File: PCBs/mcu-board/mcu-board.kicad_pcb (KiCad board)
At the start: 2 copper layers, 6 parts, among them J1 ENCODER-PANEL-1, J2 ENCODER-PANEL-2, J3 5V, J4 3.3V, J5 MDAC-INPUT-SELECTOR, U1 m0-express

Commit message: Updating mcu-board PCB
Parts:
- removed J3: 5V, Connector_Molex:Molex_KK-254_AE-6410-02A_1x02_P2.54mm_Vertical
- removed J4: 3.3V, Connector_Molex:Molex_KK-254_AE-6410-02A_1x02_P2.54mm_Vertical
- added 3.3V1: 3.3V, Connector_Molex:Molex_KK-254_AE-6410-02A_1x02_P2.54mm_Vertical, F.Cu at (153.7, 67.9)
- added 5V1: 5V, Connector_Molex:Molex_KK-254_AE-6410-02A_1x02_P2.54mm_Vertical, F.Cu at (187.3, 60.3)
- added C1: C, Capacitor_SMD:C_1206_3216Metric_Pad1.42x1.75mm_HandSolder, B.Cu at (189.2, 87.6)
- added C2: C, Capacitor_SMD:C_1206_3216Metric_Pad1.42x1.75mm_HandSolder, F.Cu at (181.6, 76.8)
- added H1: MountingHole_Pad, MountingHole:MountingHole_3.2mm_M3_Pad, F.Cu at (194.5, 100.0)
- added H2: MountingHole_Pad, MountingHole:MountingHole_3.2mm_M3_Pad, F.Cu at (153.0, 100.0)
- added H3: MountingHole_Pad, MountingHole:MountingHole_3.2mm_M3_Pad, F.Cu at (194.5, 60.0)
- added H4: MountingHole_Pad, MountingHole:MountingHole_3.2mm_M3_Pad, F.Cu at (153.0, 60.0)
- added IR1: Conn_01x03, Connector_Molex:Molex_KK-254_AE-6410-03A_1x03_P2.54mm_Vertical, F.Cu at (181.0, 67.9)
- added LED_3V1: LED, LED_SMD:LED_1206_3216Metric_Pad1.42x1.75mm_HandSolder, F.Cu at (161.9, 59.1)
- added LED_5V1: LED, LED_SMD:LED_1206_3216Metric_Pad1.42x1.75mm_HandSolder, F.Cu at (172.7, 59.1)
- added RLED1: R, Resistor_SMD:R_1206_3216Metric_Pad1.42x1.75mm_HandSolder, F.Cu at (161.9, 62.9)
- added RLED2: R, Resistor_SMD:R_1206_3216Metric_Pad1.42x1.75mm_HandSolder, F.Cu at (172.7, 62.9)
- added U2: SN74AHCT125DR, Package_SO:SOIC-14_3.9x8.7mm_P1.27mm, F.Cu at (184.2, 87.6)
- added U3: SN74AHCT125DR, Package_SO:SOIC-14_3.9x8.7mm_P1.27mm, B.Cu at (184.2, 76.8)
- added VBAT1: V-BAT, Connector_Molex:Molex_KK-254_AE-6410-02A_1x02_P2.54mm_Vertical, F.Cu at (181.0, 60.3)
- moved J1 75.8 mm to (194.3, 82.5), turned to 270 degrees
- moved J2 64.2 mm to (194.3, 67.3), turned to 270 degrees
- moved J5 35.3 mm to (153.7, 80.6), turned to 270 degrees
- moved U1 0.23 mm to (167.6, 85.7)
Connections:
- J1 pad 1: Net-(J1-Pad1) -> GND
- J1 pad 2: Net-(J1-Pad2) -> +5V
- J1 pad 3: Net-(J1-Pad3) -> encoder_1_neopixel_5v
- J1 pad 4: Net-(J1-Pad4) -> encoder_1_A_5v
- J1 pad 5: Net-(J1-Pad5) -> encoder_1_B_5v
- J2 pad 1: Net-(J2-Pad1) -> GND
- J2 pad 2: Net-(J2-Pad2) -> +5V
- J2 pad 3: Net-(J2-Pad3) -> encoder_2_neopixel_5v
- J2 pad 4: Net-(J2-Pad4) -> encoder_2_A_5v
- J2 pad 5: Net-(J2-Pad5) -> encoder_2_B_5v
- J5 pad 1: Net-(J5-Pad1) -> GND
- J5 pad 2: Net-(J5-Pad2) -> +3V3
- J5 pad 3: Net-(J5-Pad3) -> CS_input_selector
- J5 pad 4: Net-(J5-Pad4) -> SCK
- J5 pad 5: Net-(J5-Pad5) -> CS_mdac_attenuator
- J5 pad 6: Net-(J5-Pad6) -> MOSI
- U1 pad 10: Net-(U1-Pad10) -> CS_mdac_attenuator
- U1 pad 11: Net-(U1-Pad11) -> SCK
- U1 pad 12: Net-(U1-Pad12) -> MOSI
- U1 pad 19: Net-(U1-Pad19) -> encoder_1_B_3v
- U1 pad 2: Net-(U1-Pad2) -> +3V3
- U1 pad 20: Net-(U1-Pad20) -> encoder_1_A_3v
- U1 pad 21: Net-(U1-Pad21) -> encoder_1_neopixel_3v
- U1 pad 22: Net-(U1-Pad22) -> encoder_2_B_3v
- U1 pad 23: Net-(U1-Pad23) -> encoder_2_A_3v
- U1 pad 24: Net-(U1-Pad24) -> encoder_2_neopixel_3v
- U1 pad 25: Net-(U1-Pad25) -> IR_SENSOR
- U1 pad 26: Net-(U1-Pad26) -> +5V
- U1 pad 27: Net-(U1-Pad27) -> GND
- U1 pad 28: Net-(U1-Pad28) -> BAT
- U1 pad 9: Net-(U1-Pad9) -> CS_input_selector
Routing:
- net +3V3: track 0.00 -> 117.7 mm, vias 0 -> 1
- net +5V: track 0.00 -> 72.9 mm, vias 0 -> 1
- net encoder_1_neopixel_5v: track 0.00 -> 18.1 mm
- net encoder_2_neopixel_5v: track 0.00 -> 16.5 mm
- net encoder_2_A_5v: track 0.00 -> 16.2 mm
- net encoder_1_A_5v: track 0.00 -> 15.2 mm
- net IR_SENSOR: track 0.00 -> 15.1 mm
- net encoder_1_neopixel_3v: track 0.00 -> 14.6 mm
- net encoder_2_B_3v: track 0.00 -> 13.4 mm
- net BAT: track 0.00 -> 12.2 mm
- net encoder_2_B_5v: track 0.00 -> 11.4 mm
- net encoder_1_B_3v: track 0.00 -> 11.3 mm
- net encoder_1_B_5v: track 0.00 -> 10.5 mm
- net encoder_2_neopixel_3v: track 0.00 -> 10.3 mm
- net SCK: track 0.00 -> 9.57 mm
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- added copper zone on B.Cu, net GND
- added copper zone on F.Cu, net GND
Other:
- board outline added: 50.5 x 49 mm
- net class Default: clearance 0.2 -> 0.1524; trace_width 0.25 -> 0.4
- net class power added: clearance 0.1524, trace_width 0.7, via_dia 0.8, via_drill 0.4
- rule trace_clearance: 0.2 -> 0.1524

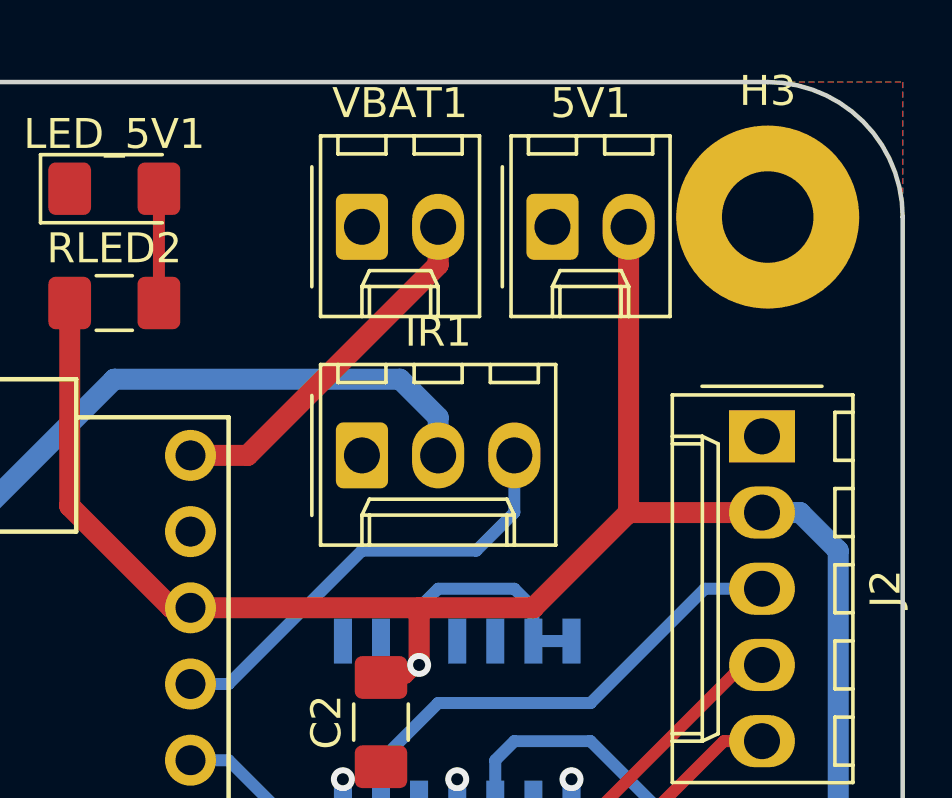
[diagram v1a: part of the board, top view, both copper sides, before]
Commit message: renaming some nets
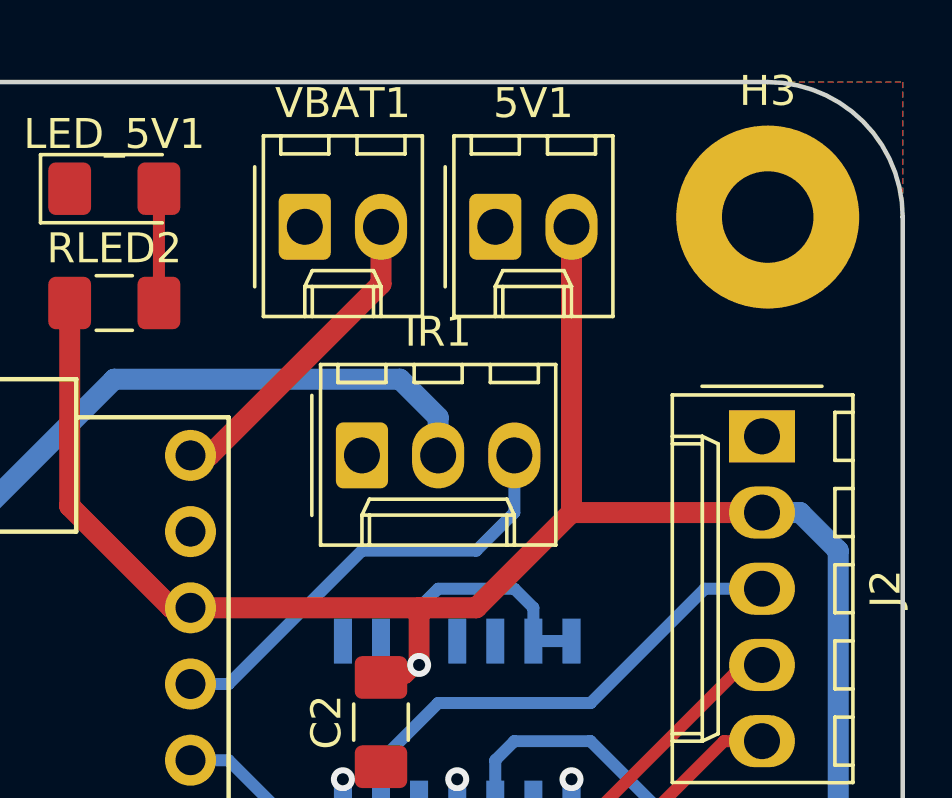
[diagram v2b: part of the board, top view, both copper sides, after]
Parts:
- moved 5V1 1.91 mm to (185.4, 60.3)
- moved VBAT1 1.91 mm to (179.1, 60.3)
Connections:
- net encoder_1_A_3v renamed panel_1_encoder_A_3v
- net encoder_1_A_5v renamed panel_1_encoder_A_5v
- net encoder_1_B_3v renamed panel_1_encoder_B_3v
- net encoder_1_B_5v renamed panel_1_encoder_B_5v
- net encoder_1_neopixel_3v renamed panel_1_neopixel_3v
- net encoder_1_neopixel_5v renamed panel_1_neopixel_5v
- net encoder_2_A_3v renamed panel_2_encoder_A_3v
- net encoder_2_A_5v renamed panel_2_encoder_A_5v
- net encoder_2_B_3v renamed panel_2_encoder_B_3v
- net encoder_2_B_5v renamed panel_2_encoder_B_5v
- net encoder_2_neopixel_3v renamed panel_2_neopixel_3v
- net encoder_2_neopixel_5v renamed panel_2_neopixel_5v
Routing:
- net BAT: track 12.2 -> 10.6 mm

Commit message: starting to fix silkscreen
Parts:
- removed J1: ENCODER-PANEL-1, Connector_Molex:Molex_KK-254_AE-6410-05A_1x05_P2.54mm_Vertical
- removed J2: ENCODER-PANEL-2, Connector_Molex:Molex_KK-254_AE-6410-05A_1x05_P2.54mm_Vertical
- added ENCODER-PANEL-1: ENCODER-PANEL-1, Connector_Molex:Molex_KK-254_AE-6410-05A_1x05_P2.54mm_Vertical, F.Cu at (194.3, 82.5)
- added ENCODER-PANEL-2: ENCODER-PANEL-2, Connector_Molex:Molex_KK-254_AE-6410-05A_1x05_P2.54mm_Vertical, F.Cu at (194.3, 67.3)
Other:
- rule trace_min: 0.2 -> 0.1524
- rule via_min_drill: 0.3 -> 0.3302
- rule via_min_size: 0.4 -> 0.6858
- board text added: "Adafruit ItsyBitsy M0 Express"
- board text added: "attenuator/selector"
- board text added: "futuresharks@gmail.com"
- board text added: "mcu-board v1.0"

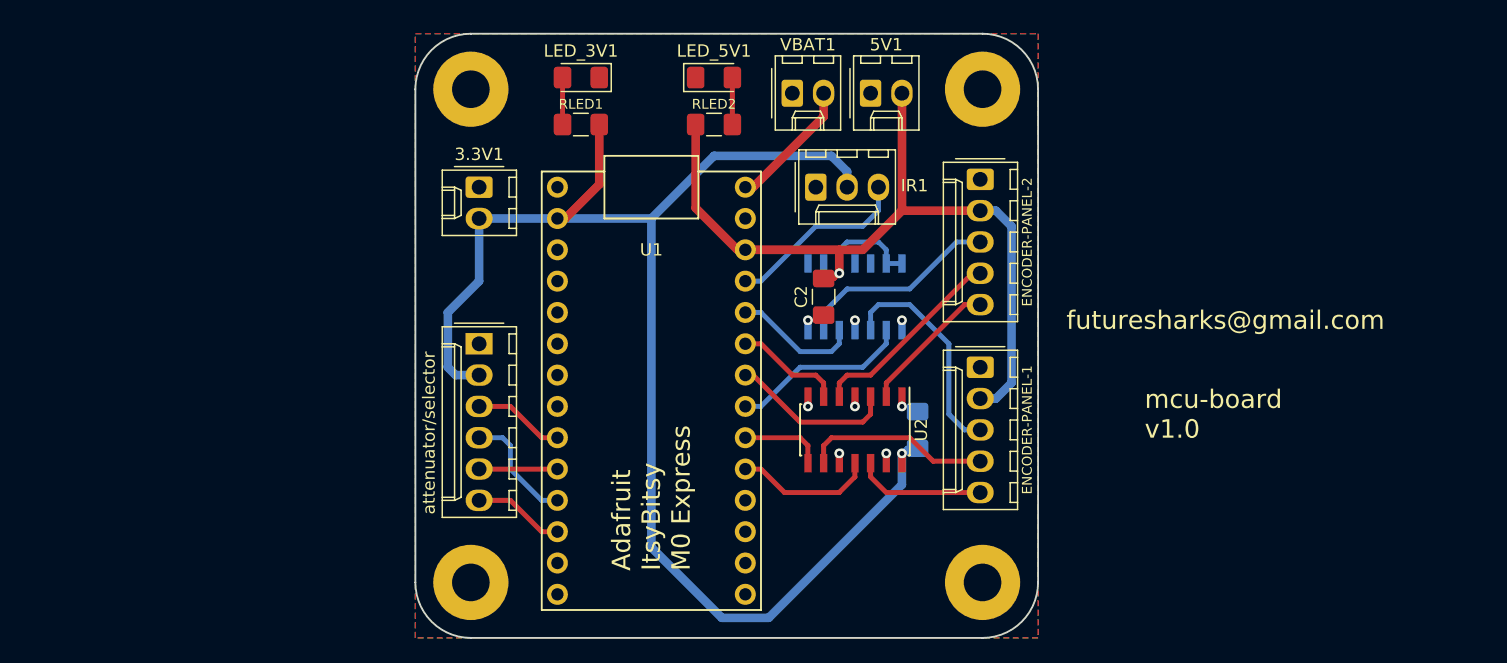
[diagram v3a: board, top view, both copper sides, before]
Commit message: change pad/mask clearance
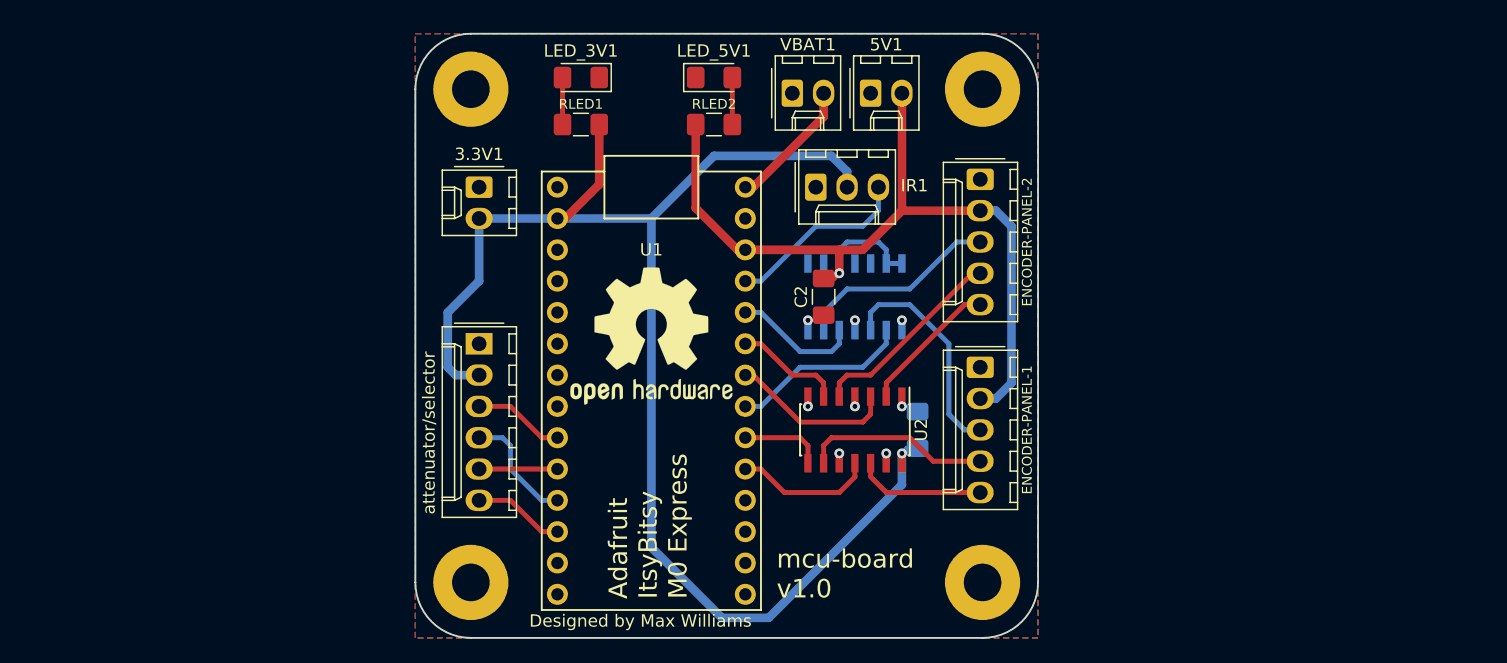
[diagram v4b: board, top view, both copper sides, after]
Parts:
- added LOGO1: Logo_Open_Hardware_Small, Symbol:OSHW-Logo2_14.6x12mm_SilkScreen, F.Cu at (167.6, 80.0)
- added LOGO2: Logo_Open_Hardware_Small, Symbol:OSHW-Logo2_14.6x12mm_SilkScreen, B.Cu at (167.6, 69.8)
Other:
- rule pad_to_mask_clearance: 0.2 -> 0.0508
- board text added: "Designed by Max Williams"
- board text added: "github.com/FutureSharks/preamp-two"

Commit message: misc updates
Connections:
- ENCODER-PANEL-2 pad 4: panel_2_encoder_A_5v -> panel_2_encoder_B_5v
- ENCODER-PANEL-2 pad 5: panel_2_encoder_B_5v -> panel_2_encoder_A_5v
- U1 pad 22: panel_2_encoder_B_3v -> panel_2_encoder_A_3v
- U1 pad 23: panel_2_encoder_A_3v -> panel_2_encoder_B_3v
- U2 pad 2: panel_2_encoder_B_5v -> panel_2_encoder_A_5v
- U2 pad 3: panel_2_encoder_B_3v -> panel_2_encoder_A_3v
- U2 pad 5: panel_2_encoder_A_5v -> panel_2_encoder_B_5v
- U2 pad 6: panel_2_encoder_A_3v -> panel_2_encoder_B_3v
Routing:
- net panel_2_encoder_B_5v: track 11.4 -> 16.2 mm
- net panel_2_encoder_A_5v: track 16.2 -> 11.4 mm
- net panel_2_encoder_B_3v: track 13.4 -> 8.78 mm
- net panel_2_encoder_A_3v: track 8.78 -> 13.4 mm
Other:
- board text added: "+"
- board text added: "3.3V"
- board text added: "5V"
- board text added: "GND"
- board text added: "IR"
- board text added: "VBAT"
